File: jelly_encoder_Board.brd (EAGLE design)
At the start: 78.3 x 79.9 mm, 4 parts, among them IC1 IC-MU150_DFN16-5X5, J1 SM05B-SRSS-TB(LF)(SN), J2 S5B-PH-SM4-TB(LF)(SN)

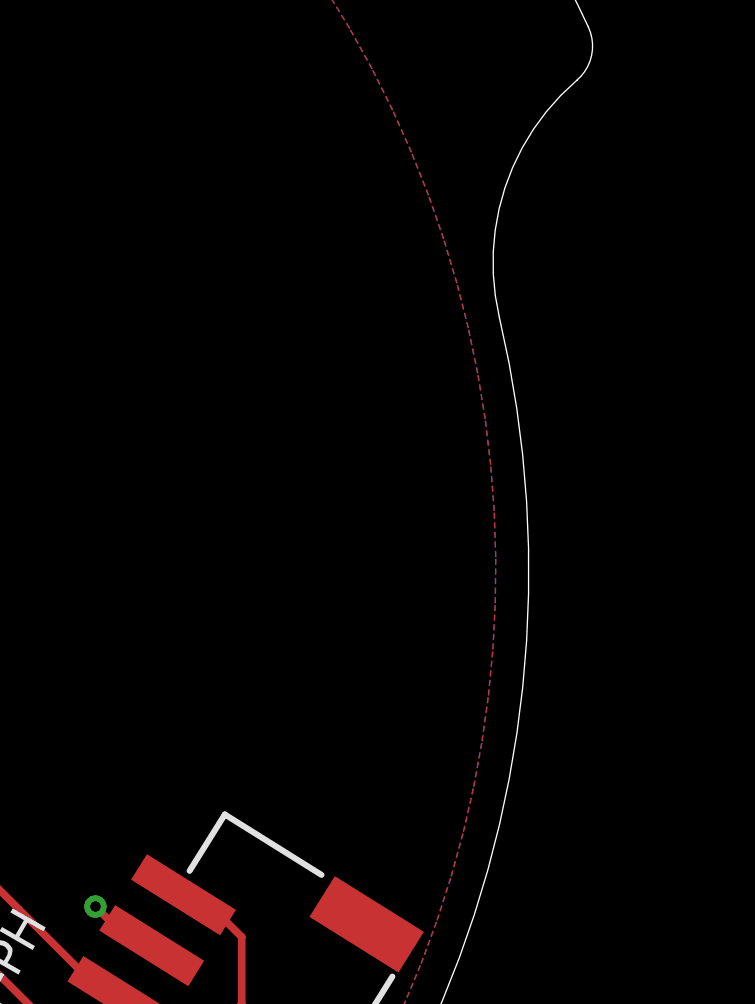
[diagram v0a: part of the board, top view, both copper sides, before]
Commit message: added RGB Sensor pins
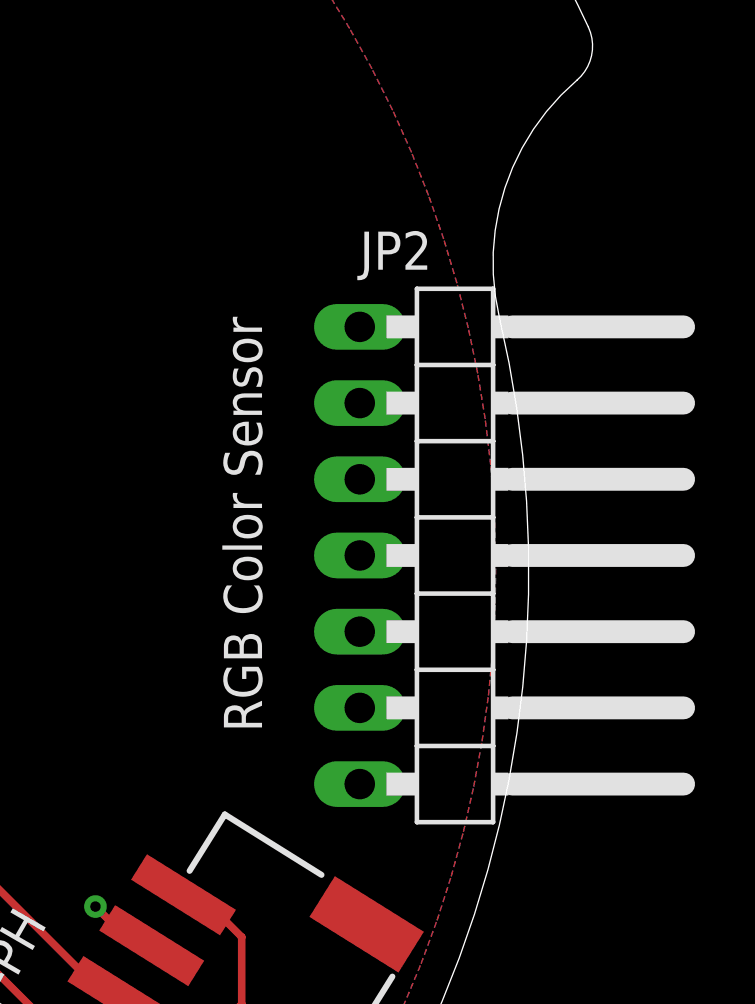
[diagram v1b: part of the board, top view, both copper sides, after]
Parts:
- added JP2: (no value), pinhead:1X07/90
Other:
- board text added: "RGB Color Sensor"
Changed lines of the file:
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@@
 <text x="18.4221625" y="-16.158590625" size="1.27" layer="21" rot="R60">JST-PH</text>
 <text x="-23.772309375" y="-16.59978125" size="1.27" layer="21" rot="R300">JST-SR</text>
+<text x="28.10746875" y="-5.3593875" size="1.27" layer="21" rot="R90">RGB Color Sensor</text>
 </plain>
 <attributes>
@@
 <attribute name="RS_PRICE-STOCK" value="" x="25.490603125" y="-10.782840625" size="1.778" layer="27" rot="R238" display="off"/>
 </element>
+<element name="JP2" library="pinhead" library_urn="urn:adsk.eagle:library:325" package="1X07/90" package3d_urn="urn:adsk.eagle:package:22476/2" value="" x="35.175765625" y="0.526940625" rot="R270"/>
 </elements>
 <signals>

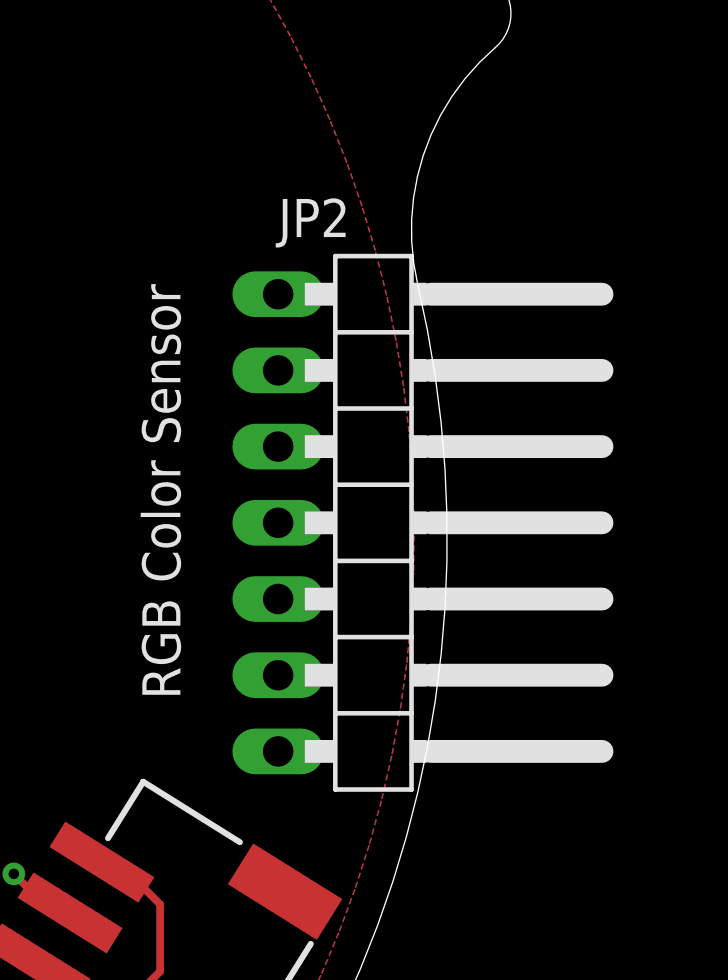
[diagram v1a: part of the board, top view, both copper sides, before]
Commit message: added RGB Sensor pins
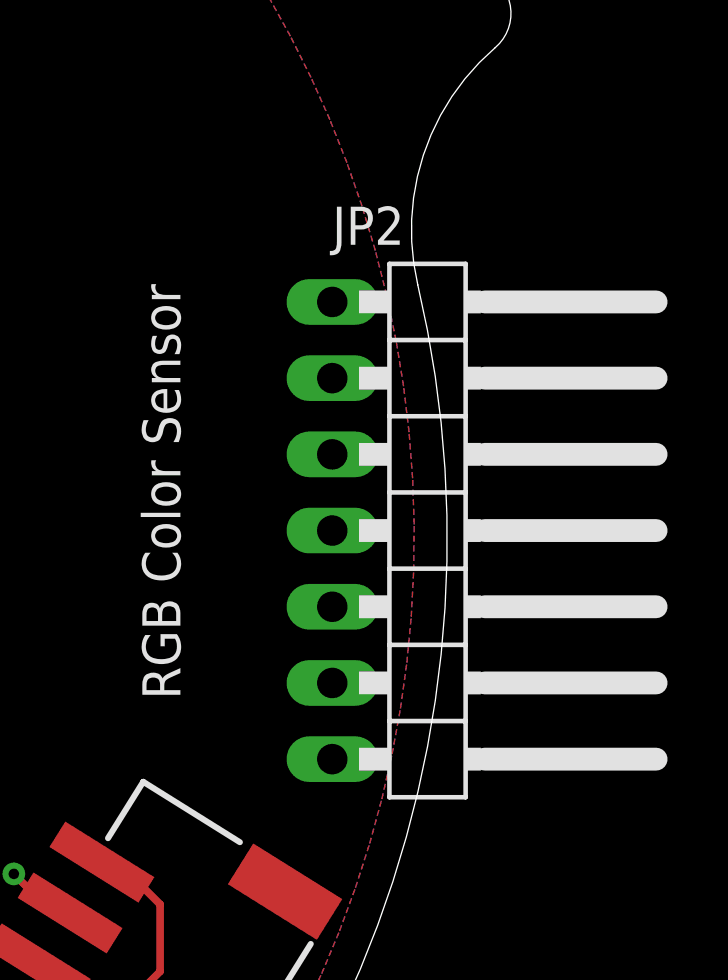
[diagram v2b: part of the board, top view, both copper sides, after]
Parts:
- moved JP2 1.82 mm to (37.0, 0.27)
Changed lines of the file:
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@@
 <attribute name="RS_PRICE-STOCK" value="" x="25.490603125" y="-10.782840625" size="1.778" layer="27" rot="R238" display="off"/>
 </element>
-<element name="JP2" library="pinhead" library_urn="urn:adsk.eagle:library:325" package="1X07/90" package3d_urn="urn:adsk.eagle:package:22476/2" value="" x="35.175765625" y="0.526940625" rot="R270"/>
+<element name="JP2" library="pinhead" library_urn="urn:adsk.eagle:library:325" package="1X07/90" package3d_urn="urn:adsk.eagle:package:22476/2" value="" x="36.97956875" y="0.2688875" rot="R270"/>
 </elements>
 <signals>

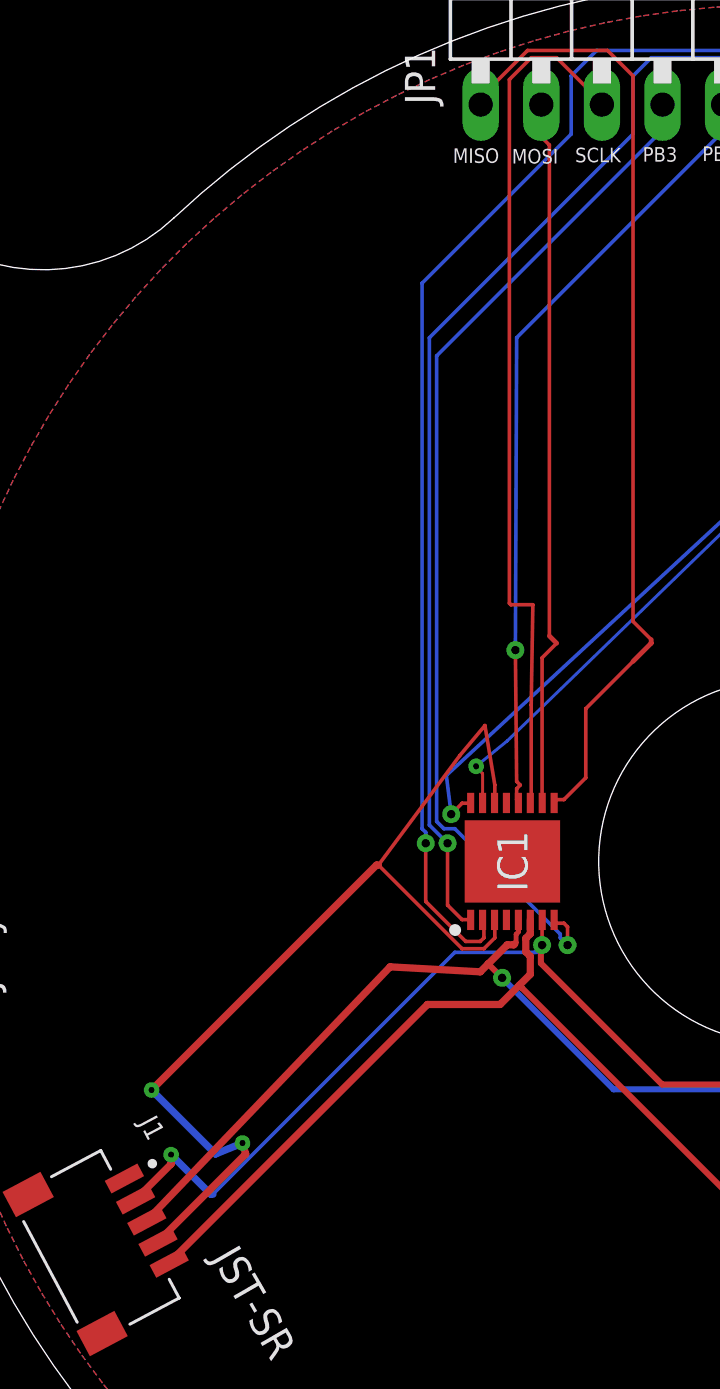
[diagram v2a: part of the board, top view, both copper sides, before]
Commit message: fixed traces and added decoupling caps
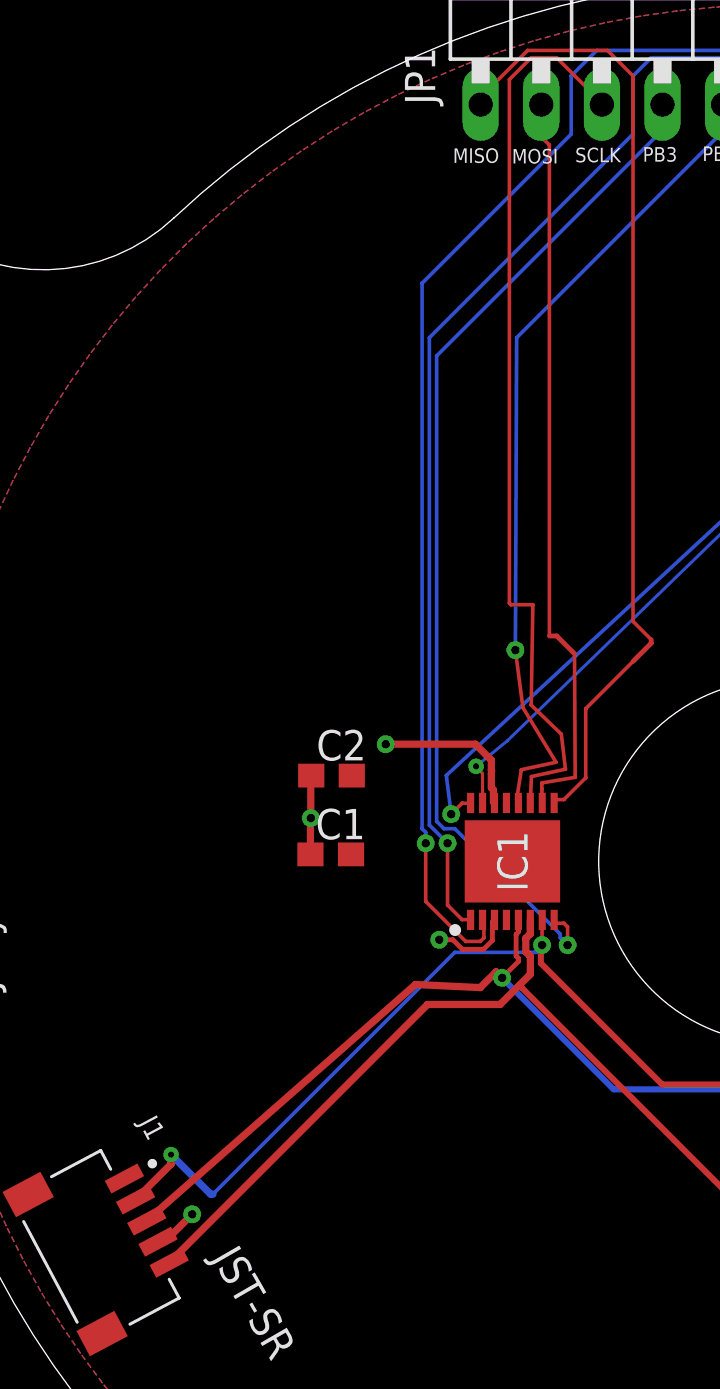
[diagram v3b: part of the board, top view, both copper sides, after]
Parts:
- added C1, C2: .1uF, resistor:C0603
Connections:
- net GND: now also C1.2, C2.2
- net VCC: now also C1.1, C2.1
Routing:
- net VCC: track 44.4 -> 17.7 mm, vias 3 -> 5
- net SCLK: track 36.4 -> 38.1 mm
- net PA0: track 33.0 -> 34.5 mm
- net MOSI: track 29.8 -> 31.2 mm
- net A: track 61.3 -> 60.7 mm

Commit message: fixed layout and other things
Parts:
- moved C1 16.8 mm to (-32.3, -9.53), turned to 300 degrees
- moved C2 14.6 mm to (-28.5, -7.30), turned to 300 degrees
- moved JP2 0.71 mm to (36.3, 0.18), turned to 260 degrees
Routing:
- net GND: track 0.00 -> 3.39 mm
- net VCC: track 17.7 -> 18.8 mm
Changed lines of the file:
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@@
 <text x="18.4221625" y="-16.158590625" size="1.27" layer="21" rot="R60">JST-PH</text>
 <text x="-23.772309375" y="-16.59978125" size="1.27" layer="21" rot="R300">JST-SR</text>
-<text x="28.10746875" y="-5.3593875" size="1.27" layer="21" rot="R90">RGB Color Sensor</text>
+<text x="32.762034375" y="13.8862875" size="1.27" layer="21" rot="R170">RGB Color Sensor</text>
 </plain>
 <attributes>
@@
 <attribute name="RS_PRICE-STOCK" value="" x="25.490603125" y="-10.782840625" size="1.778" layer="27" rot="R238" display="off"/>
 </element>
-<element name="JP2" library="pinhead" library_urn="urn:adsk.eagle:library:325" package="1X07/90" package3d_urn="urn:adsk.eagle:package:22476/2" value="" x="36.97956875" y="0.2688875" rot="R270"/>
-<element name="C1" library="resistor" library_urn="urn:adsk.eagle:library:348" package="C0603" package3d_urn="urn:adsk.eagle:package:26138/1" value=".1uF" x="-18.76288125" y="0.294321875"/>
-<element name="C2" library="resistor" library_urn="urn:adsk.eagle:library:348" package="C0603" package3d_urn="urn:adsk.eagle:package:26138/1" value=".1uF" x="-18.730734375" y="3.59728125"/>
+<element name="JP2" library="pinhead" library_urn="urn:adsk.eagle:library:325" package="1X07/90" package3d_urn="urn:adsk.eagle:package:22476/2" value="" x="36.276990625" y="0.18100625" rot="R260"/>
+<element name="C1" library="resistor" library_urn="urn:adsk.eagle:library:348" package="C0603" package3d_urn="urn:adsk.eagle:package:26138/1" value=".1uF" x="-32.33794375" y="-9.529921875" rot="R300"/>
+<element name="C2" library="resistor" library_urn="urn:adsk.eagle:library:348" package="C0603" package3d_urn="urn:adsk.eagle:package:26138/1" value=".1uF" x="-28.517378125" y="-7.300146875" rot="R300"/>
 </elements>
 <signals>
 <signal name="GND">
-<polygon width="0.3048" layer="1" isolate="0.00030625" thermals="no">
+<polygon width="0.3048" layer="1" isolate="0.00030625">
 <vertex x="25.4" y="25.4" curve="197.492324"/>
 <vertex x="-16.51" y="-31.75" curve="162.507676"/>
@@
 <contactref element="C2" pad="2"/>
 <contactref element="C1" pad="2"/>
+<wire x1="-11.4006" y1="-2.45" x2="-11.4006" y2="-3.320803125" width="0.2032" layer="1"/>
+<wire x1="-11.4006" y1="-3.320803125" x2="-11.4414875" y2="-3.361690625" width="0.2032" layer="1"/>
+<wire x1="-11.4006" y1="2.45" x2="-11.4006" y2="1.36716875" width="0.2032" layer="1"/>
+<wire x1="-11.4006" y1="1.36716875" x2="-11.3141875" y2="1.28075625" width="0.2032" layer="1"/>
+<wire x1="-11.4006" y1="-2.45" x2="-11.399578125" y2="-2.448978125" width="0.2032" layer="1"/>
+<wire x1="-11.399578125" y1="-2.448978125" x2="-11.399578125" y2="-1.195375" width="0.2032" layer="1"/>
 </signal>
 <signal name="VCC">
@@
 <contactref element="C2" pad="1"/>
 <contactref element="C1" pad="1"/>
-<polygon width="0.4826" layer="16" isolate="0.00030625" thermals="no">
+<polygon width="0.4826" layer="16" isolate="0.00030625">
 <vertex x="25.4" y="25.4" curve="197.492324"/>
 <vertex x="-16.51" y="-31.75" curve="162.507676"/>
 </polygon>
-<wire x1="-19.61288125" y1="0.294321875" x2="-19.61288125" y2="1.804925" width="0.3048" layer="1"/>
-<wire x1="-19.61288125" y1="1.804925" x2="-19.5997125" y2="1.81809375" width="0.3048" layer="1"/>
-<via x="-19.5997125" y="1.81809375" extent="1-16" drill="0.35"/>
-<wire x1="-19.5997125" y1="1.81809375" x2="-19.5997125" y2="3.578303125" width="0.3048" layer="1"/>
-<wire x1="-19.5997125" y1="3.578303125" x2="-19.580734375" y2="3.59728125" width="0.3048" layer="1"/>
+<wire x1="-32.76294375" y1="-8.7938" x2="-31.692646875" y2="-8.17994375" width="0.3048" layer="1"/>
+<wire x1="-31.692646875" y1="-8.17994375" x2="-30.78465625" y2="-7.58338125" width="0.3048" layer="1"/>
+<via x="-30.78465625" y="-7.58338125" extent="1-16" drill="0.35"/>
+<wire x1="-30.78465625" y1="-7.58338125" x2="-29.971690625" y2="-7.107740625" width="0.3048" layer="1"/>
+<wire x1="-29.971690625" y1="-7.107740625" x2="-28.942378125" y2="-6.564025" width="0.3048" layer="1"/>
 <wire x1="-26.00151875" y1="-15.93563125" x2="-25.720515625" y2="-15.93563125" width="0.3048" layer="1"/>
 <wire x1="-25.720515625" y1="-15.93563125" x2="-24.571859375" y2="-14.786975" width="0.3048" layer="1"/>
